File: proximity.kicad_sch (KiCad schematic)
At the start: 19 parts, among them J1 Conn_01x04_Male, SW1 SW_Push, SW2 SW_SPDT, U1 AMS1117-3.3, U2 HC-SR04, U3 STM32L011D3Px, Y1 2MHz

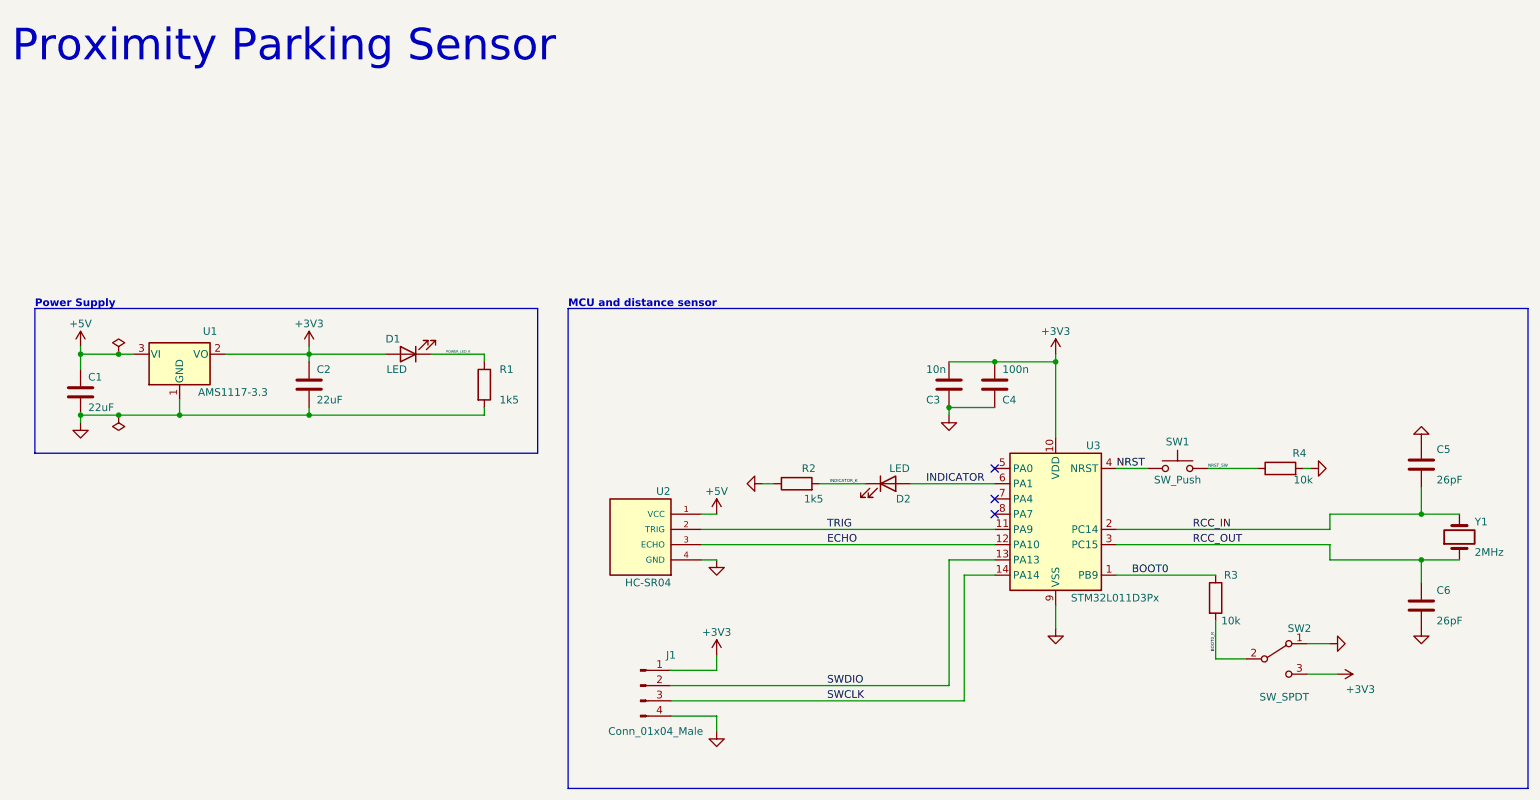
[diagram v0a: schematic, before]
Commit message: Update to ST VL35LXX distance sensor
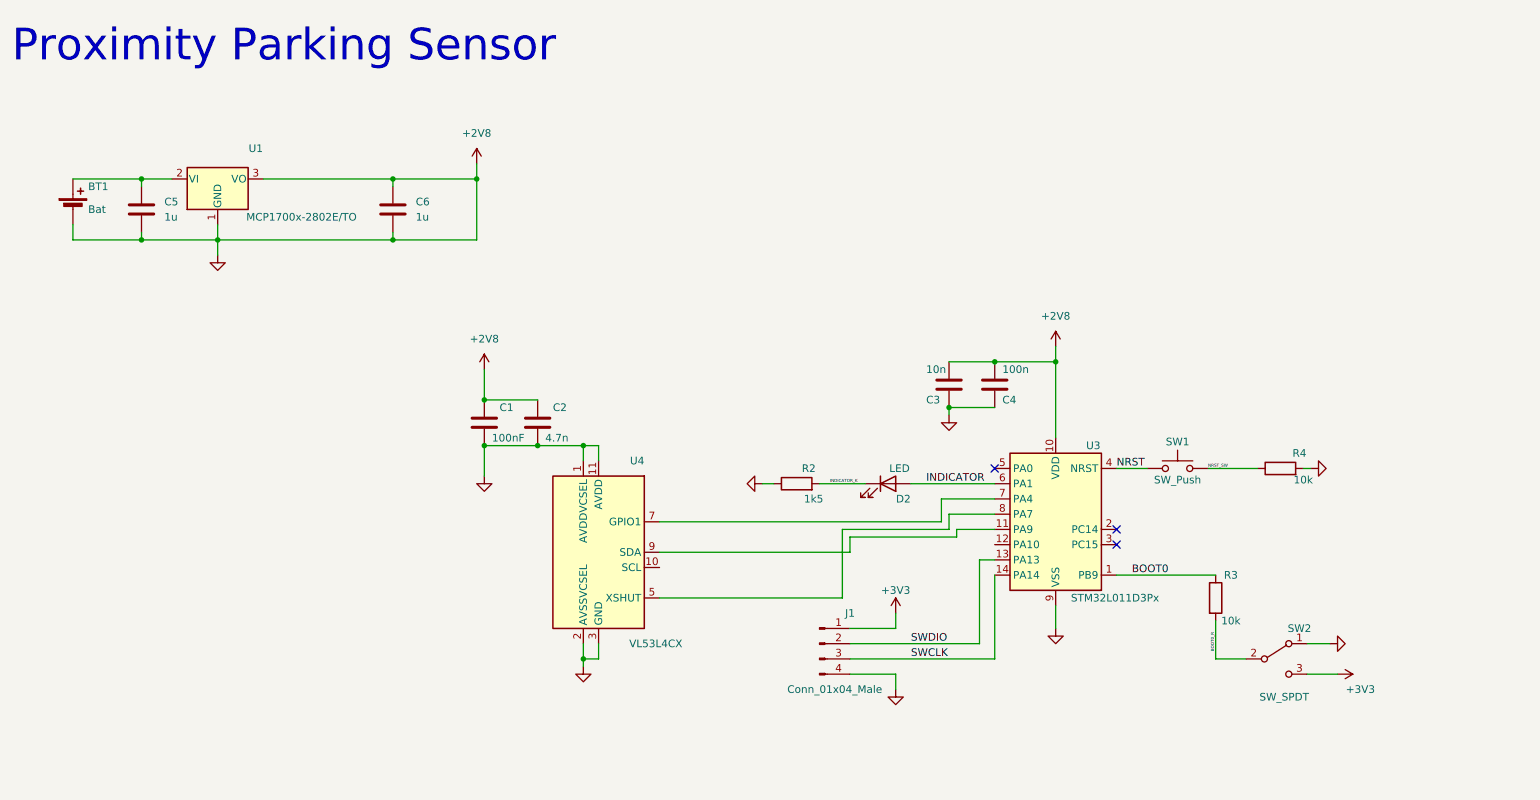
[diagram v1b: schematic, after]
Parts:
- removed D1: LED, symbol Device:LED
- removed R1: 1k5, symbol Device:R
- removed U1: AMS1117-3.3, Package_TO_SOT_SMD:SOT-223-3_TabPin2, symbol Regulator_Linear:AMS1117-3.3
- removed U2: HC-SR04, XCVR_HC-SR04, symbol HC-SR04:HC-SR04
- removed Y1: 2MHz, symbol Device:Crystal
- added BT1: Bat, symbol Device:Battery_Cell
- added U1: MCP1700x-2802E/TO, Package_TO_SOT_THT:TO-92_Inline, symbol Regulator_Linear:MCP1700x-280xxTO
- added U4: VL53L4CX, Sensor_Distance:ST_VL53L1x, symbol Sensor_Distance:VL53L1CXV0FY1
- C1: value 22uF -> 100nF
- C2: value 22uF -> 4.7n
- C5, C6: value 26pF -> 1u
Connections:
- net +3V3: no longer C2.1, C3.2, C4.2, U3.10 (VDD)
- net at U3.7 (PA4): now also U4.7 (GPIO1)
- net at U3.8 (PA7): now also U4.5 (XSHUT)
- net +5V renamed +2V8
- net +2V8: now also C1.2, C2.1, C2.2, C3.1, C3.2, C4.1, C4.2, C5.2, C6.1, C6.2, J1.4 (Pin_4), R2.1, R4.2, SW2.1 (A), U3.10 (VDD), U3.9 (VSS), BT1.2 (-), U1.1 (GND), U1.3 (VO), U4.1 (AVDDVCSEL), U4.11 (AVDD), U4.12 (GND), U4.2 (AVSSVCSEL), U4.3 (GND), U4.4 (GND), U4.6 (GND)
- net ECHO: no longer names the net of U3.12 (PA10)
- removed net GND: C1.2, C2.2, C3.1, C4.1, C5.1, C6.2, J1.4 (Pin_4), R2.1, R4.2, SW2.1 (A), U3.9 (VSS)
- net RCC_IN: no longer names the net of U3.2 (PC14)
- net RCC_IN: no longer C5.2
- net RCC_OUT: no longer names the net of U3.3 (PC15)
- net RCC_OUT: no longer C6.1
- net TRIG: no longer names the net of U3.11 (PA9)
- net TRIG: now also U4.9 (SDA)
- new net: BT1.1 (+), C5.1, U1.2 (VI)
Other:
- note removed: "MCU and distance sensor"
- note removed: "Power Supply"
- moved on the sheet: J1
